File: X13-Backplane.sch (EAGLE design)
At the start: 38 parts, among them J1 PXC-PTSM-04-RA-1778641, J2 284512-4, J3 284512-8, J4 PXC-PTSM-04-RA-1778641, J5 PXC-PTSM-04-RA-1778641, J6 284512-4, J8 284512-8, T1 284512-3, T2 284512-3, T3 284512-3, T4 284512-3, T5 284512-3, T6 284512-3, T7 284512-3, T8 284512-3

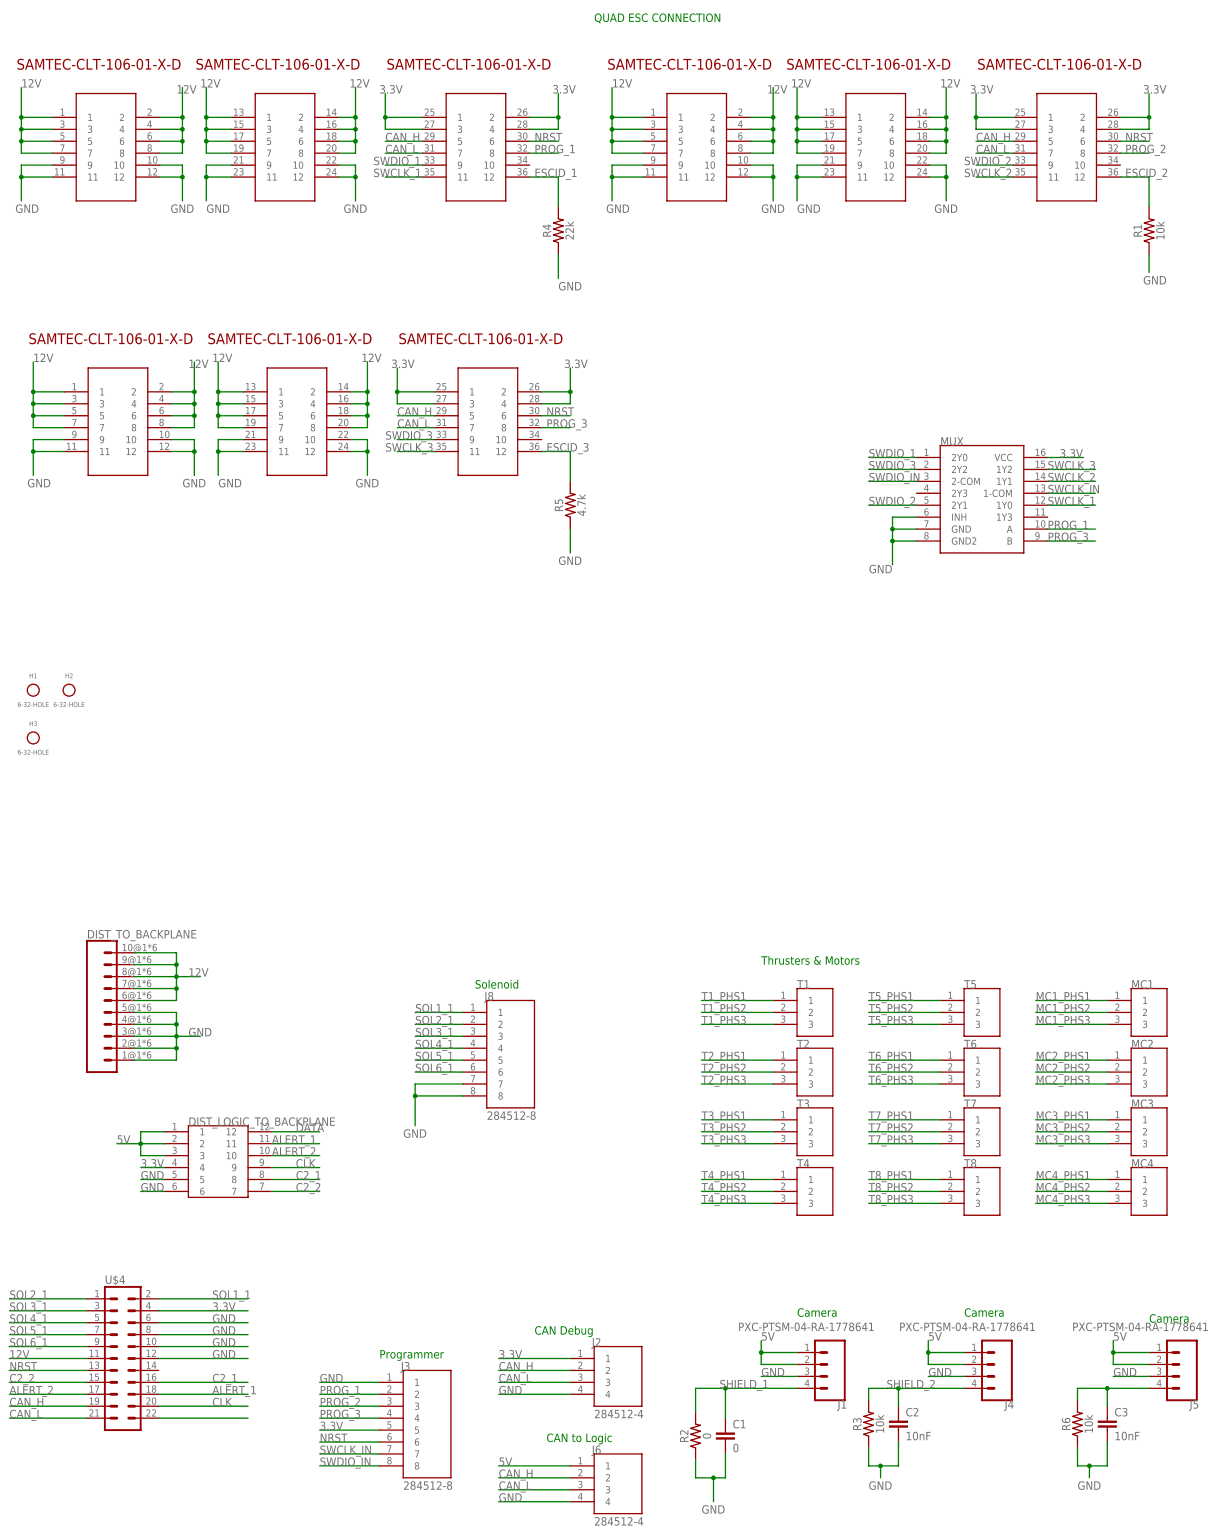
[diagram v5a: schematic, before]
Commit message: updated board layout and connections
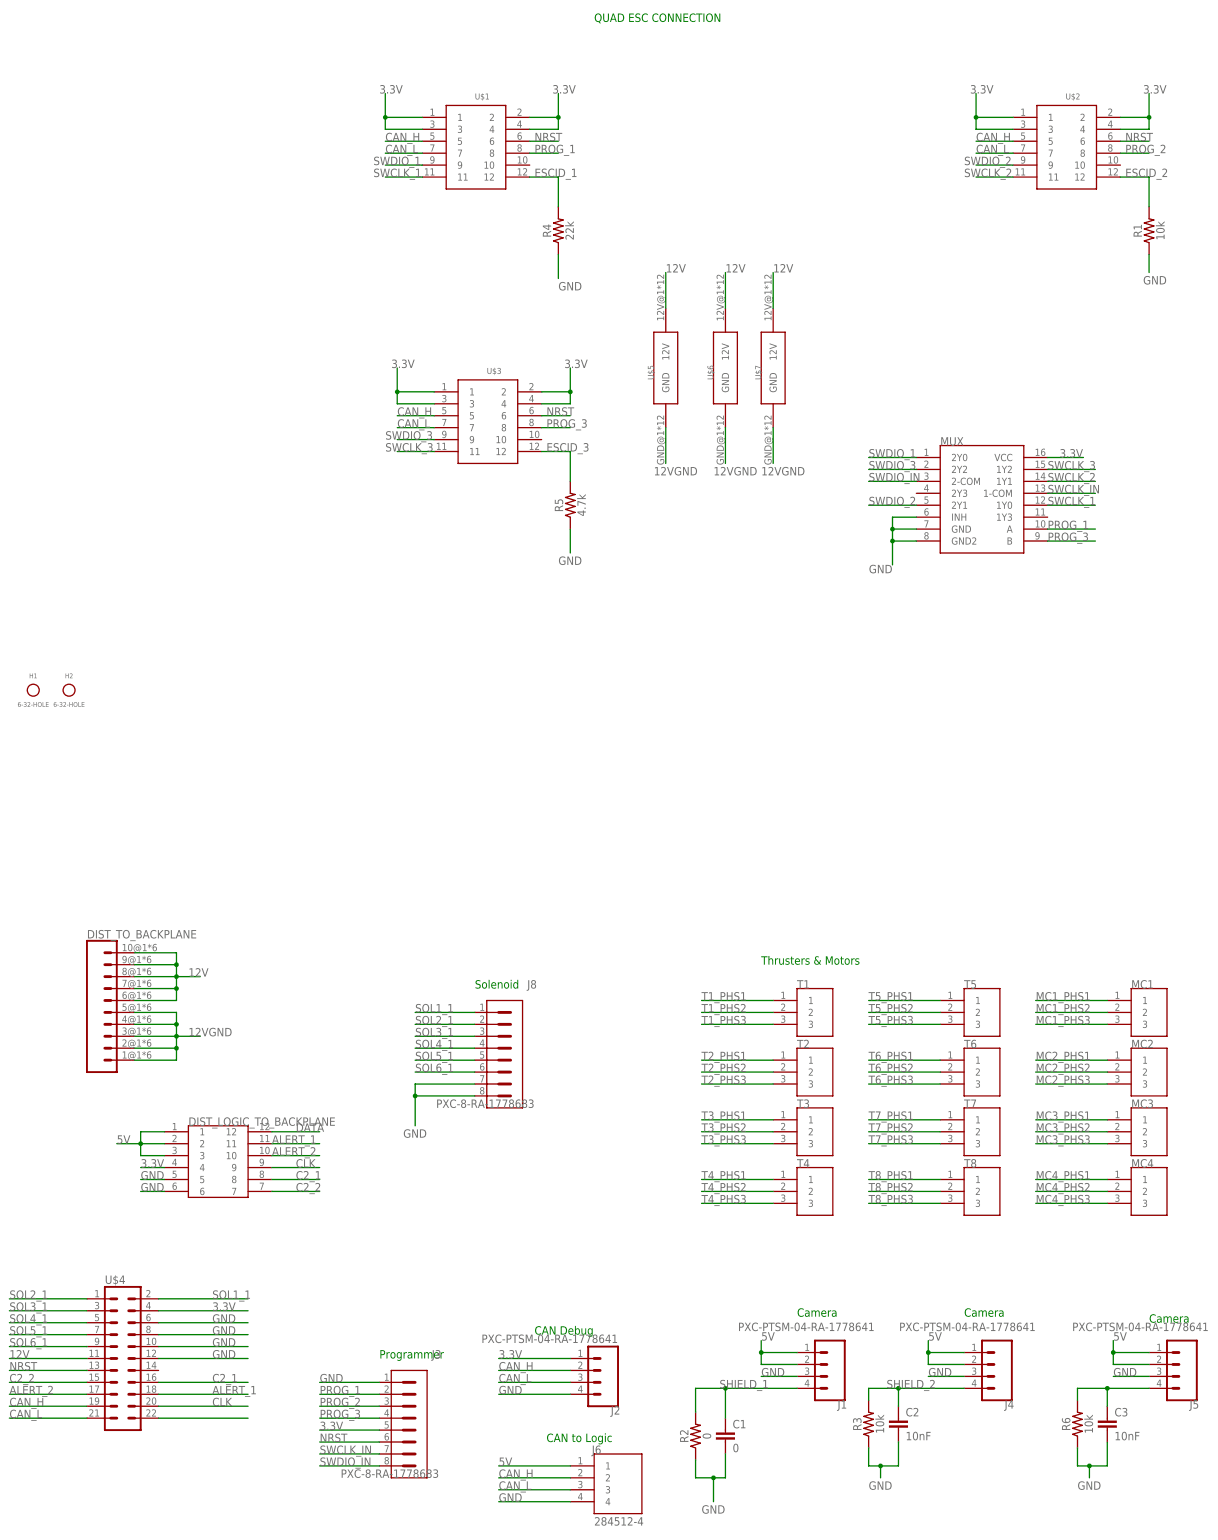
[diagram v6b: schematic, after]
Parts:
- removed H3: 6-32-HOLE, Mounting Holes:6-32-HOLE
- added U$5, U$6, U$7: BACKPLANE_ESC_ADAPTER_PWRBKP, Backplane_ESC_adapter:BACKPLANE_ESC_ADAPTER_PWRBKP
- DIST_LOGIC_TO_BACKPLANE: value IPL1-107-01-L-D-RE-P -> IPL1-106-01-L-D-K; device Backplane_Dist_Logic_Connector:IPL1-107-01-L-D-RE-P -> Backplane_Dist_Logic_Connector:IPL1-106-01-L-D-K
- J2: value 284512-4 -> PXC-PTSM-04-RA-1778641; device 284512-4:284512-4 -> Phoenix Contact PTSM-04-V-1778573:PXC-PTSM-04-RA-1778641
- J3, J8: value 284512-8 -> PXC-8-RA-1778683; device 284512-8:284512-8 -> Phoenix Contact PTSM 8 pin:PXC-8-RA-1778683
- U$1, U$2, U$3: value BACKPLANE_CONNECTORS -> BACKPLANE_CONNECTORSBKP; device BLHeli_32 45A:BACKPLANE_CONNECTORS -> BLHeli_32 45A:BACKPLANE_CONNECTORSBKP
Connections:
- new net 12VGND: DIST_TO_BACKPLANE.1, DIST_TO_BACKPLANE.2, DIST_TO_BACKPLANE.3, DIST_TO_BACKPLANE.4, DIST_TO_BACKPLANE.5, U$5.GND, U$6.GND, U$7.GND
- net 12V: now also U$5.12V, U$6.12V, U$7.12V; no longer U$1G$1.1, U$1G$1.2, U$1G$1.3, U$1G$1.4, U$1G$1.5, U$1G$1.6, U$1G$1.7, U$1G$1.8, U$1G$2.1, U$1G$2.2, U$1G$2.3, U$1G$2.4, U$1G$2.5, U$1G$2.6, U$1G$2.7, U$1G$2.8, U$2G$1.1, U$2G$1.2, U$2G$1.3, U$2G$1.4, U$2G$1.5, U$2G$1.6, U$2G$1.7, U$2G$1.8, U$2G$2.1, U$2G$2.2, U$2G$2.3, U$2G$2.4, U$2G$2.5, U$2G$2.6, U$2G$2.7, U$2G$2.8, U$3G$1.1, U$3G$1.2, U$3G$1.3, U$3G$1.4, U$3G$1.5, U$3G$1.6, U$3G$1.7, U$3G$1.8, U$3G$2.1, U$3G$2.2, U$3G$2.3, U$3G$2.4, U$3G$2.5, U$3G$2.6, U$3G$2.7, U$3G$2.8
- net 3.3V: now also U$1.1, U$1.2, U$1.3, U$1.4, U$2.1, U$2.2, U$2.3, U$2.4, U$3.1, U$3.2, U$3.3, U$3.4; no longer U$1G$3.1, U$1G$3.2, U$1G$3.3, U$1G$3.4, U$2G$3.1, U$2G$3.2, U$2G$3.3, U$2G$3.4, U$3G$3.1, U$3G$3.2, U$3G$3.3, U$3G$3.4
- net CAN_H: now also U$1.5, U$2.5, U$3.5; no longer U$1G$3.5, U$2G$3.5, U$3G$3.5
- net CAN_L: now also U$1.7, U$2.7, U$3.7; no longer U$1G$3.7, U$2G$3.7, U$3G$3.7
- net ESCID_1: now also U$1.12; no longer U$1G$3.12
- net ESCID_2: now also U$2.12; no longer U$2G$3.12
- net ESCID_3: now also U$3.12; no longer U$3G$3.12
- net GND: no longer DIST_TO_BACKPLANE.1, DIST_TO_BACKPLANE.2, DIST_TO_BACKPLANE.3, DIST_TO_BACKPLANE.4, DIST_TO_BACKPLANE.5, U$1G$1.10, U$1G$1.11, U$1G$1.12, U$1G$1.9, U$1G$2.10, U$1G$2.11, U$1G$2.12, U$1G$2.9, U$2G$1.10, U$2G$1.11, U$2G$1.12, U$2G$1.9, U$2G$2.10, U$2G$2.11, U$2G$2.12, U$2G$2.9, U$3G$1.10, U$3G$1.11, U$3G$1.12, U$3G$1.9, U$3G$2.10, U$3G$2.11, U$3G$2.12, U$3G$2.9
- net NRST: now also U$1.6, U$2.6, U$3.6; no longer U$1G$3.6, U$2G$3.6, U$3G$3.6
- net PROG_1: now also U$1.8; no longer U$1G$3.8
- net PROG_2: now also U$2.8; no longer U$2G$3.8
- net PROG_3: now also U$3.8; no longer U$3G$3.8
- net SWCLK_1: now also U$1.11; no longer U$1G$3.11
- net SWCLK_2: now also U$2.11; no longer U$2G$3.11
- net SWCLK_3: now also U$3.11; no longer U$3G$3.11
- net SWDIO_1: now also U$1.9; no longer U$1G$3.9
- net SWDIO_2: now also U$2.9; no longer U$2G$3.9
- net SWDIO_3: now also U$3.9; no longer U$3G$3.9
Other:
- moved on the sheet: J2

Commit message: updated board
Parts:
- removed MC1, MC2, MC3, MC4, T1, T2, T3, T4, T5, T6, T7, T8: 284512-3, ThrusterConnector:284512-3
- added C4: .1uF, SparkFun-Capacitors:10NF-0603-50V-10%
- added C5: 47uF, Panasonic 47 uF cap - EEE-1CA470SP:47UF-POLAR-PANASONIC_D-35V-20%
- added D1, D2, D3, D4: 0.5A/40V/420mV, SparkFun-DiscreteSemi:DIODE-SCHOTTKY-PMEG4005EJ
- added R7, R8: 60, SparkFun-Resistors:68.1KOHM-0603-1/10W-1%
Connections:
- removed net DATA1: U$4.22
- removed net MC1_PHS1: MC1.1
- removed net MC1_PHS2: MC1.2
- removed net MC1_PHS3: MC1.3
- removed net MC2_PHS1: MC2.1
- removed net MC2_PHS2: MC2.2
- removed net MC2_PHS3: MC2.3
- removed net MC3_PHS1: MC3.1
- removed net MC3_PHS2: MC3.2
- removed net MC3_PHS3: MC3.3
- removed net MC4_PHS1: MC4.1
- removed net MC4_PHS2: MC4.2
- removed net MC4_PHS3: MC4.3
- removed net T1_PHS1: T1.1
- removed net T1_PHS2: T1.2
- removed net T1_PHS3: T1.3
- removed net T2_PHS1: T2.1
- removed net T2_PHS2: T2.2
- removed net T2_PHS3: T2.3
- removed net T3_PHS1: T3.1
- removed net T3_PHS2: T3.2
- removed net T3_PHS3: T3.3
- removed net T4_PHS1: T4.1
- removed net T4_PHS2: T4.2
- removed net T4_PHS3: T4.3
- removed net T5_PHS1: T5.1
- removed net T5_PHS2: T5.2
- removed net T5_PHS3: T5.3
- removed net T6_PHS1: T6.1
- removed net T6_PHS2: T6.2
- removed net T6_PHS3: T6.3
- removed net T7_PHS1: T7.1
- removed net T7_PHS2: T7.2
- removed net T7_PHS3: T7.3
- removed net T8_PHS1: T8.1
- removed net T8_PHS2: T8.2
- removed net T8_PHS3: T8.3
- new net N$3: C4.1, R7.1, R8.2
- new net NRST_1: D1.A, U$1.6
- new net NRST_2: D2.A, U$2.6
- new net NRST_3: D3.A, U$3.6
- new net NRST_4: D4.A, U$4.13
- net 12V: now also C5.+, J8.1, J8.2
- net CAN_H: now also R7.2
- net CAN_L: now also R8.1
- net DATA: now also U$4.22
- net GND: now also C4.2, C5.-; no longer J8.7, J8.8
- net NRST: now also D1.C, D2.C, D3.C, D4.C; no longer U$1.6, U$2.6, U$3.6, U$4.13
- net PROG_1: no longer U$1.8
- net PROG_2: no longer U$2.8
- net PROG_3: no longer U$3.8
- net SOL1_1: now also J8.8; no longer J8.1
- net SOL2_1: now also J8.7; no longer J8.2
- net SOL3_1: now also J8.6; no longer J8.3
- net SOL4_1: now also J8.5; no longer J8.4
- net SOL5_1: now also J8.4; no longer J8.5
- net SOL6_1: now also J8.3; no longer J8.6
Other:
- note removed: "Thrusters & Motors"

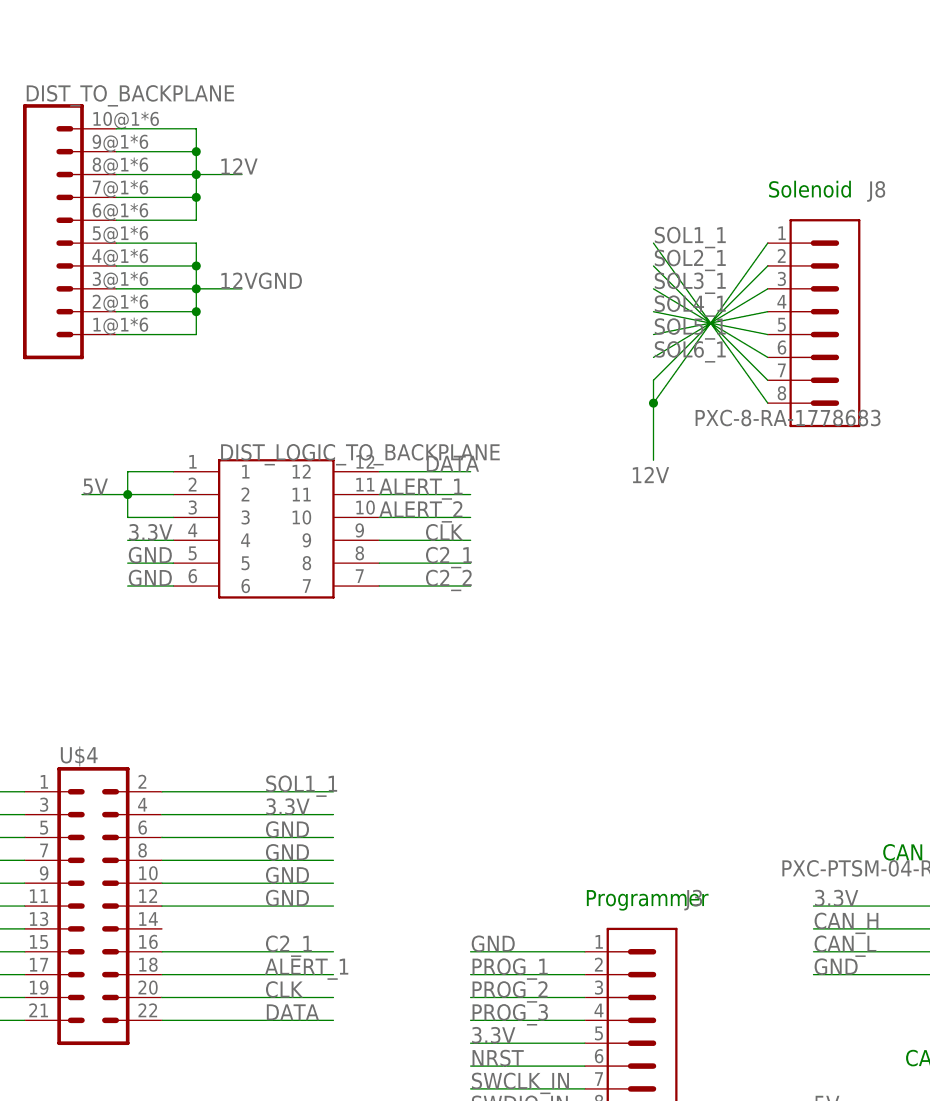
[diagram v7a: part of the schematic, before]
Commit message: added swclk/swdio signals to solenoid board
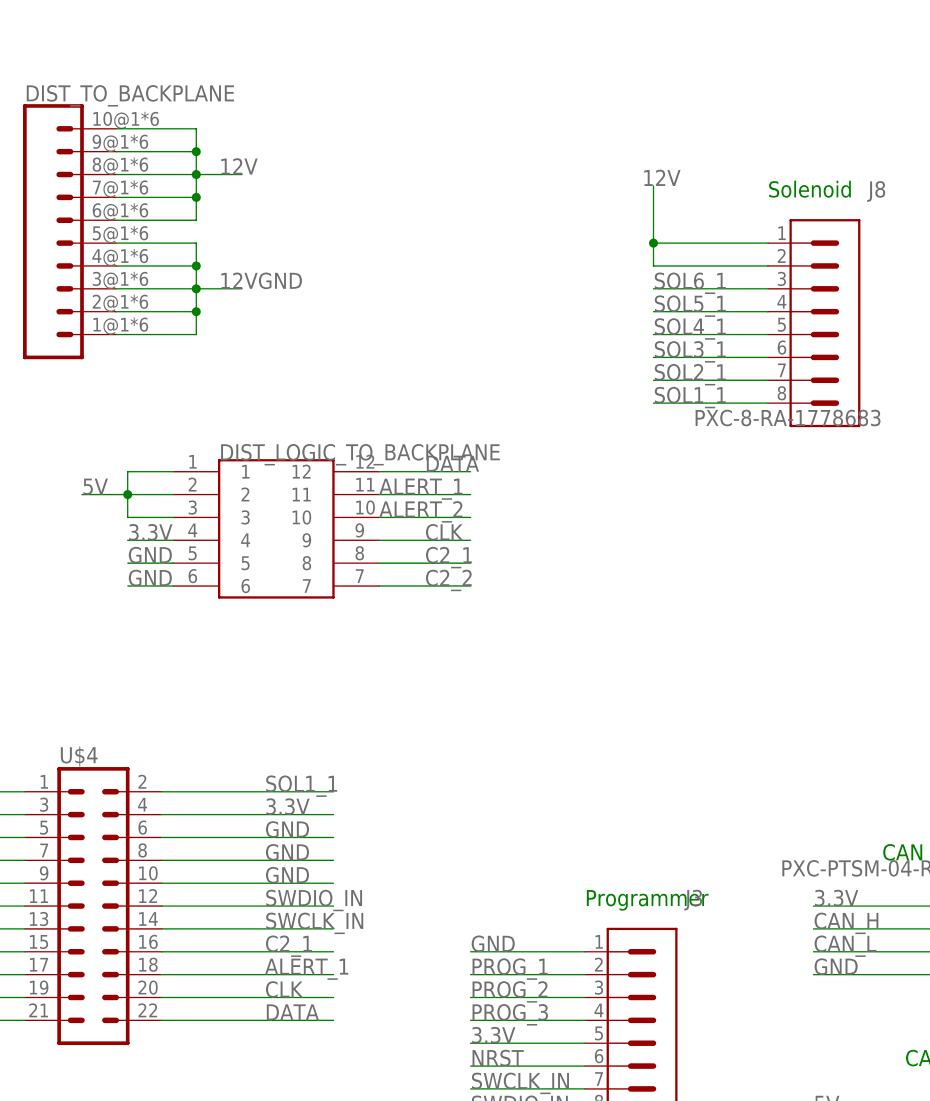
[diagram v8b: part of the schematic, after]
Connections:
- net GND: no longer U$4.12
- net SWCLK_IN: now also U$4.14
- net SWDIO_IN: now also U$4.12
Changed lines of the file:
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@@
-</segment>
-<segment>
-<wire x1="-257.81" y1="-106.68" x2="-238.76" y2="-106.68" width="0.1524" layer="91"/>
-<label x="-246.38" y="-106.68" size="1.778" layer="95"/>
-<pinref part="U$4" gate="G$1" pin="12"/>
 </segment>
 <segment>
@@
 </segment>
 <segment>
-<pinref part="J8" gate="G$1" pin="2"/>
-<wire x1="-190.5" y1="-35.56" x2="-203.2" y2="-48.26" width="0.1524" layer="91"/>
-<wire x1="-203.2" y1="-48.26" x2="-203.2" y2="-50.8" width="0.1524" layer="91"/>
-<pinref part="J8" gate="G$1" pin="1"/>
-<wire x1="-203.2" y1="-50.8" x2="-203.2" y2="-57.15" width="0.1524" layer="91"/>
-<wire x1="-190.5" y1="-33.02" x2="-203.2" y2="-50.8" width="0.1524" layer="91"/>
-<junction x="-203.2" y="-50.8"/>
-<label x="-205.74" y="-59.69" size="1.778" layer="95"/>
-</segment>
-<segment>
 <pinref part="C5" gate="G$1" pin="+"/>
 <wire x1="-158.75" y1="-57.15" x2="-158.75" y2="-66.04" width="0.1524" layer="91"/>
 <label x="-156.21" y="-67.31" size="1.778" layer="95" rot="R180"/>
 </segment>
+<segment>
+<pinref part="J8" gate="G$1" pin="2"/>
+<wire x1="-190.5" y1="-35.56" x2="-203.2" y2="-35.56" width="0.1524" layer="91"/>
+<wire x1="-203.2" y1="-35.56" x2="-203.2" y2="-33.02" width="0.1524" layer="91"/>
+<pinref part="J8" gate="G$1" pin="1"/>
+<wire x1="-203.2" y1="-33.02" x2="-203.2" y2="-26.67" width="0.1524" layer="91"/>
+<wire x1="-190.5" y1="-33.02" x2="-203.2" y2="-33.02" width="0.1524" layer="91"/>
+<junction x="-203.2" y="-33.02"/>
+<label x="-204.47" y="-26.67" size="1.778" layer="95"/>
+</segment>
 </net>
 <net name="SWCLK_IN" class="0">
@@
 <label x="-223.52" y="-127" size="1.778" layer="95"/>
 </segment>
+<segment>
+<pinref part="U$4" gate="G$1" pin="14"/>
+<wire x1="-257.81" y1="-109.22" x2="-238.76" y2="-109.22" width="0.1524" layer="91"/>
+<label x="-246.38" y="-109.22" size="1.778" layer="95"/>
+</segment>
 </net>
 <net name="SWDIO_IN" class="0">
@@
 <wire x1="-210.82" y1="-129.54" x2="-223.52" y2="-129.54" width="0.1524" layer="91"/>
 <label x="-223.52" y="-129.54" size="1.778" layer="95"/>
+</segment>
+<segment>
+<wire x1="-257.81" y1="-106.68" x2="-238.76" y2="-106.68" width="0.1524" layer="91"/>
+<label x="-246.38" y="-106.68" size="1.778" layer="95"/>
+<pinref part="U$4" gate="G$1" pin="12"/>
 </segment>
 </net>
@@
 <segment>
 <pinref part="J8" gate="G$1" pin="7"/>
-<wire x1="-190.5" y1="-48.26" x2="-203.2" y2="-35.56" width="0.1524" layer="91"/>
-<label x="-203.2" y="-35.56" size="1.778" layer="95"/>
+<wire x1="-190.5" y1="-48.26" x2="-203.2" y2="-48.26" width="0.1524" layer="91"/>
+<label x="-203.2" y="-48.26" size="1.778" layer="95"/>
 </segment>
 <segment>
@@
 <segment>
 <pinref part="J8" gate="G$1" pin="6"/>
-<wire x1="-190.5" y1="-45.72" x2="-203.2" y2="-38.1" width="0.1524" layer="91"/>
-<label x="-203.2" y="-38.1" size="1.778" layer="95"/>
+<wire x1="-190.5" y1="-45.72" x2="-203.2" y2="-45.72" width="0.1524" layer="91"/>
+<label x="-203.2" y="-45.72" size="1.778" layer="95"/>
 </segment>
 <segment>
@@
 <segment>
 <pinref part="J8" gate="G$1" pin="5"/>
-<wire x1="-190.5" y1="-43.18" x2="-203.2" y2="-40.64" width="0.1524" layer="91"/>
-<label x="-203.2" y="-40.64" size="1.778" layer="95"/>
+<wire x1="-190.5" y1="-43.18" x2="-203.2" y2="-43.18" width="0.1524" layer="91"/>
+<label x="-203.2" y="-43.18" size="1.778" layer="95"/>
 </segment>
 <segment>
@@
 <segment>
 <pinref part="J8" gate="G$1" pin="4"/>
-<wire x1="-190.5" y1="-40.64" x2="-203.2" y2="-43.18" width="0.1524" layer="91"/>
-<label x="-203.2" y="-43.18" size="1.778" layer="95"/>
+<wire x1="-190.5" y1="-40.64" x2="-203.2" y2="-40.64" width="0.1524" layer="91"/>
+<label x="-203.2" y="-40.64" size="1.778" layer="95"/>
 </segment>
 <segment>
@@
 <segment>
 <pinref part="J8" gate="G$1" pin="3"/>
-<wire x1="-190.5" y1="-38.1" x2="-203.2" y2="-45.72" width="0.1524" layer="91"/>
-<label x="-203.2" y="-45.72" size="1.778" layer="95"/>
+<wire x1="-190.5" y1="-38.1" x2="-203.2" y2="-38.1" width="0.1524" layer="91"/>
+<label x="-203.2" y="-38.1" size="1.778" layer="95"/>
 </segment>
 <segment>
@@
 <segment>
 <pinref part="J8" gate="G$1" pin="8"/>
-<wire x1="-190.5" y1="-50.8" x2="-203.2" y2="-33.02" width="0.1524" layer="91"/>
-<label x="-203.2" y="-33.02" size="1.778" layer="95"/>
-</segment>
-<segment>
+<wire x1="-190.5" y1="-50.8" x2="-203.2" y2="-50.8" width="0.1524" layer="91"/>
+<label x="-203.2" y="-50.8" size="1.778" layer="95"/>
+</segment>
+<segment>
